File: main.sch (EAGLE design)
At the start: 44 parts, among them IC1 MEGA16-A, IC2 MCP73831, IC3 7805DT, Q2 32768k

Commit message: Schematics
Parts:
- added R22: 10k, rcl:R-EU_R1206
- added S1: MODE, switch-omron:10-XX
- JP1: value (none) -> 12V
- JP2: value (none) -> BAT 3.7V
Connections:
- new net N$38: IC1.(T0/XCK)PB0, R22.1, S1.S
- net +5V: now also R22.2
- net GND: now also S1.P
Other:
- moved on the sheet: D2, R20, R21
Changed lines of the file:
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@@
 <part name="T5" library="transistor" deviceset="*-PNP-" device="SOT23-BEC" technology="BC807-25"/>
 <part name="U$1" library="dallas-1" deviceset="DS1629" device=""/>
-<part name="JP1" library="pinhead" deviceset="PINHD-1X2" device=""/>
-<part name="JP2" library="pinhead" deviceset="PINHD-1X2" device=""/>
+<part name="JP1" library="pinhead" deviceset="PINHD-1X2" device="" value="12V"/>
+<part name="JP2" library="pinhead" deviceset="PINHD-1X2" device="" value="BAT 3.7V"/>
 <part name="IC2" library="microchip-update-2" deviceset="MCP73831" device=""/>
 <part name="IC3" library="linear" deviceset="78*" device="DT" technology="05"/>
@@
 <part name="T6" library="transistor" deviceset="*-NPN-" device="SOT23-EBC"/>
 <part name="D2" library="diode" deviceset="BZX84CSMD" device=""/>
+<part name="R22" library="rcl" deviceset="R-EU_" device="R1206" value="10k"/>
+<part name="GND9" library="supply1" deviceset="GND" device=""/>
+<part name="P+7" library="supply1" deviceset="+5V" device=""/>
+<part name="S1" library="switch-omron" deviceset="10-XX" device="" value="MODE"/>
 </parts>
 <sheets>
@@
 <instance part="R19" gate="G$1" x="246.38" y="33.02"/>
 <instance part="+3V2" gate="G$1" x="213.36" y="233.68"/>
-<instance part="R20" gate="G$1" x="213.36" y="154.94" rot="R90"/>
-<instance part="R21" gate="G$1" x="213.36" y="139.7" rot="R90"/>
+<instance part="R20" gate="G$1" x="218.44" y="195.58" rot="R90"/>
+<instance part="R21" gate="G$1" x="218.44" y="180.34" rot="R90"/>
 <instance part="P+4" gate="1" x="38.1" y="195.58"/>
-<instance part="P+5" gate="1" x="213.36" y="177.8"/>
-<instance part="GND8" gate="1" x="213.36" y="124.46"/>
+<instance part="P+5" gate="1" x="218.44" y="208.28"/>
+<instance part="GND8" gate="1" x="218.44" y="165.1"/>
 <instance part="P+6" gate="1" x="134.62" y="157.48"/>
 <instance part="D3" gate="G$1" x="33.02" y="180.34"/>
@@
 <instance part="D1" gate="G$1" x="45.72" y="160.02" rot="R90"/>
 <instance part="T6" gate="G$1" x="45.72" y="177.8" rot="R90"/>
-<instance part="D2" gate="G$1" x="220.98" y="139.7" rot="R90"/>
+<instance part="D2" gate="G$1" x="226.06" y="180.34" rot="R90"/>
+<instance part="R22" gate="G$1" x="213.36" y="142.24" rot="R90"/>
+<instance part="GND9" gate="1" x="213.36" y="111.76"/>
+<instance part="P+7" gate="1" x="213.36" y="154.94"/>
+<instance part="S1" gate="1" x="213.36" y="121.92"/>
 </instances>
 <busses>
@@
 <pinref part="GND8" gate="1" pin="GND"/>
 <pinref part="R21" gate="G$1" pin="1"/>
-<wire x1="213.36" y1="127" x2="213.36" y2="132.08" width="0.1524" layer="91"/>
-<wire x1="213.36" y1="132.08" x2="213.36" y2="134.62" width="0.1524" layer="91"/>
-<wire x1="220.98" y1="137.16" x2="220.98" y2="132.08" width="0.1524" layer="91"/>
-<wire x1="220.98" y1="132.08" x2="213.36" y2="132.08" width="0.1524" layer="91"/>
-<junction x="213.36" y="132.08"/>
+<wire x1="218.44" y1="167.64" x2="218.44" y2="172.72" width="0.1524" layer="91"/>
+<wire x1="218.44" y1="172.72" x2="218.44" y2="175.26" width="0.1524" layer="91"/>
+<wire x1="226.06" y1="177.8" x2="226.06" y2="172.72" width="0.1524" layer="91"/>
+<wire x1="226.06" y1="172.72" x2="218.44" y2="172.72" width="0.1524" layer="91"/>
+<junction x="218.44" y="172.72"/>
 <pinref part="D2" gate="G$1" pin="A"/>
+</segment>
+<segment>
+<pinref part="GND9" gate="1" pin="GND"/>
+<wire x1="213.36" y1="116.84" x2="213.36" y2="114.3" width="0.1524" layer="91"/>
+<pinref part="S1" gate="1" pin="P"/>
 </segment>
 </net>
@@
 <junction x="134.62" y="132.08"/>
 </segment>
+<segment>
+<pinref part="P+7" gate="1" pin="+5V"/>
+<pinref part="R22" gate="G$1" pin="2"/>
+<wire x1="213.36" y1="152.4" x2="213.36" y2="147.32" width="0.1524" layer="91"/>
+</segment>
 </net>
 <net name="N$8" class="0">
@@
 <pinref part="P+5" gate="1" pin="+12V"/>
 <pinref part="R20" gate="G$1" pin="2"/>
-<wire x1="213.36" y1="175.26" x2="213.36" y2="160.02" width="0.1524" layer="91"/>
+<wire x1="218.44" y1="205.74" x2="218.44" y2="200.66" width="0.1524" layer="91"/>
 </segment>
 <segment>
@@
 <pinref part="R21" gate="G$1" pin="2"/>
 <pinref part="R20" gate="G$1" pin="1"/>
-<wire x1="213.36" y1="144.78" x2="213.36" y2="147.32" width="0.1524" layer="91"/>
+<wire x1="218.44" y1="185.42" x2="218.44" y2="187.96" width="0.1524" layer="91"/>
 <pinref part="IC1" gate="G$1" pin="(ADC0)PA0"/>
-<wire x1="213.36" y1="147.32" x2="213.36" y2="149.86" width="0.1524" layer="91"/>
-<wire x1="193.04" y1="134.62" x2="203.2" y2="134.62" width="0.1524" layer="91"/>
-<wire x1="203.2" y1="134.62" x2="203.2" y2="147.32" width="0.1524" layer="91"/>
-<wire x1="203.2" y1="147.32" x2="213.36" y2="147.32" width="0.1524" layer="91"/>
-<junction x="213.36" y="147.32"/>
-<wire x1="213.36" y1="147.32" x2="220.98" y2="147.32" width="0.1524" layer="91"/>
-<wire x1="220.98" y1="147.32" x2="220.98" y2="142.24" width="0.1524" layer="91"/>
+<wire x1="218.44" y1="187.96" x2="218.44" y2="190.5" width="0.1524" layer="91"/>
+<wire x1="193.04" y1="134.62" x2="198.12" y2="134.62" width="0.1524" layer="91"/>
+<wire x1="198.12" y1="134.62" x2="198.12" y2="187.96" width="0.1524" layer="91"/>
+<wire x1="198.12" y1="187.96" x2="218.44" y2="187.96" width="0.1524" layer="91"/>
+<junction x="218.44" y="187.96"/>
+<wire x1="218.44" y1="187.96" x2="226.06" y2="187.96" width="0.1524" layer="91"/>
+<wire x1="226.06" y1="187.96" x2="226.06" y2="182.88" width="0.1524" layer="91"/>
 <pinref part="D2" gate="G$1" pin="C"/>
 </segment>
@@
 <wire x1="124.46" y1="218.44" x2="129.54" y2="218.44" width="0.1524" layer="91"/>
 <wire x1="124.46" y1="218.44" x2="124.46" y2="170.18" width="0.1524" layer="91"/>
-<wire x1="124.46" y1="170.18" x2="198.12" y2="170.18" width="0.1524" layer="91"/>
+<wire x1="124.46" y1="170.18" x2="195.58" y2="170.18" width="0.1524" layer="91"/>
 <pinref part="IC1" gate="G$1" pin="(ADC7)PA7"/>
-<wire x1="198.12" y1="170.18" x2="198.12" y2="152.4" width="0.1524" layer="91"/>
-<wire x1="198.12" y1="152.4" x2="193.04" y2="152.4" width="0.1524" layer="91"/>
+<wire x1="195.58" y1="170.18" x2="195.58" y2="152.4" width="0.1524" layer="91"/>
+<wire x1="195.58" y1="152.4" x2="193.04" y2="152.4" width="0.1524" layer="91"/>
 </segment>
 </net>
@@
 </segment>
 </net>
+<net name="N$38" class="0">
+<segment>
+<pinref part="R22" gate="G$1" pin="1"/>
+<wire x1="213.36" y1="137.16" x2="213.36" y2="132.08" width="0.1524" layer="91"/>
+<pinref part="IC1" gate="G$1" pin="(T0/XCK)PB0"/>
+<wire x1="213.36" y1="132.08" x2="213.36" y2="127" width="0.1524" layer="91"/>
+<wire x1="193.04" y1="111.76" x2="203.2" y2="111.76" width="0.1524" layer="91"/>
+<wire x1="203.2" y1="111.76" x2="203.2" y2="132.08" width="0.1524" layer="91"/>
+<wire x1="203.2" y1="132.08" x2="213.36" y2="132.08" width="0.1524" layer="91"/>
+<junction x="213.36" y="132.08"/>
+<pinref part="S1" gate="1" pin="S"/>
+</segment>
+</net>

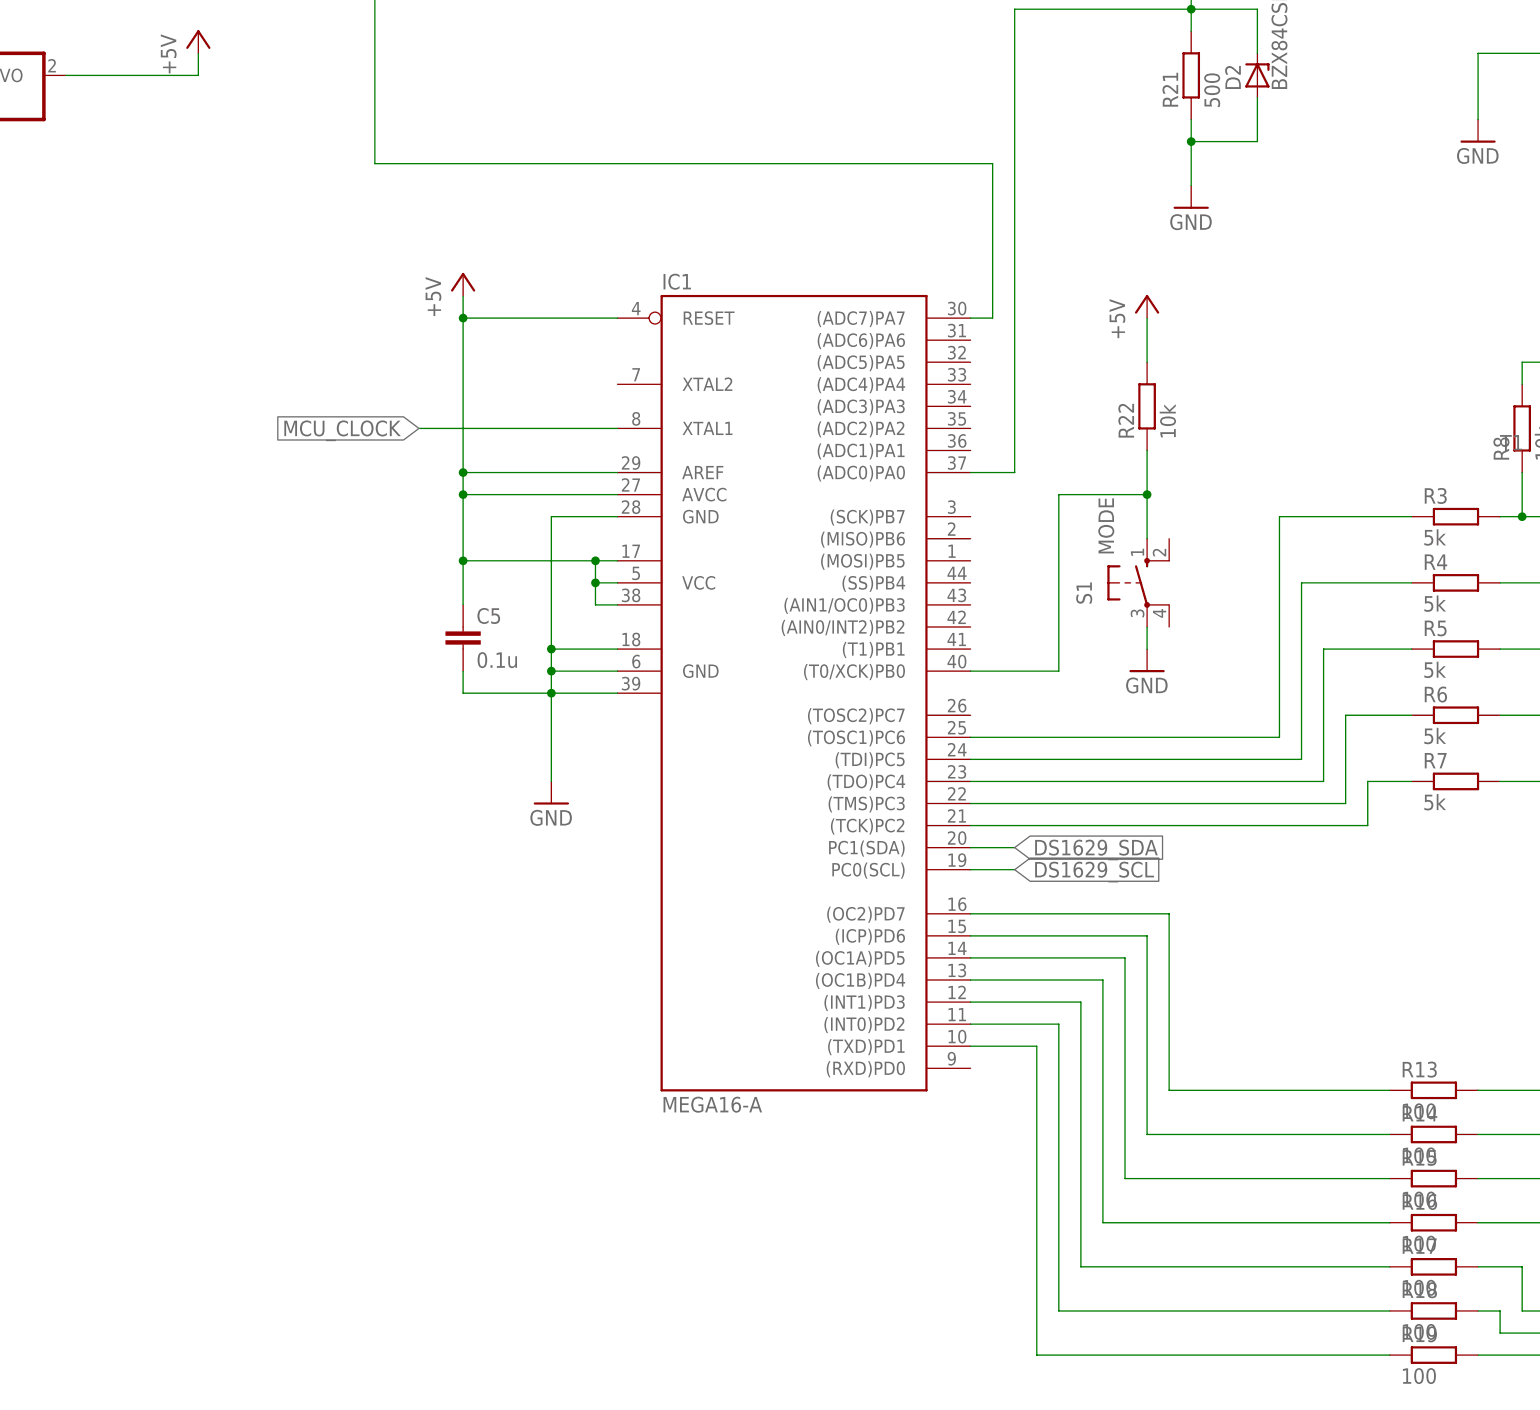
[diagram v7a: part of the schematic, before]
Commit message: Atmega8 instead of Atmega16
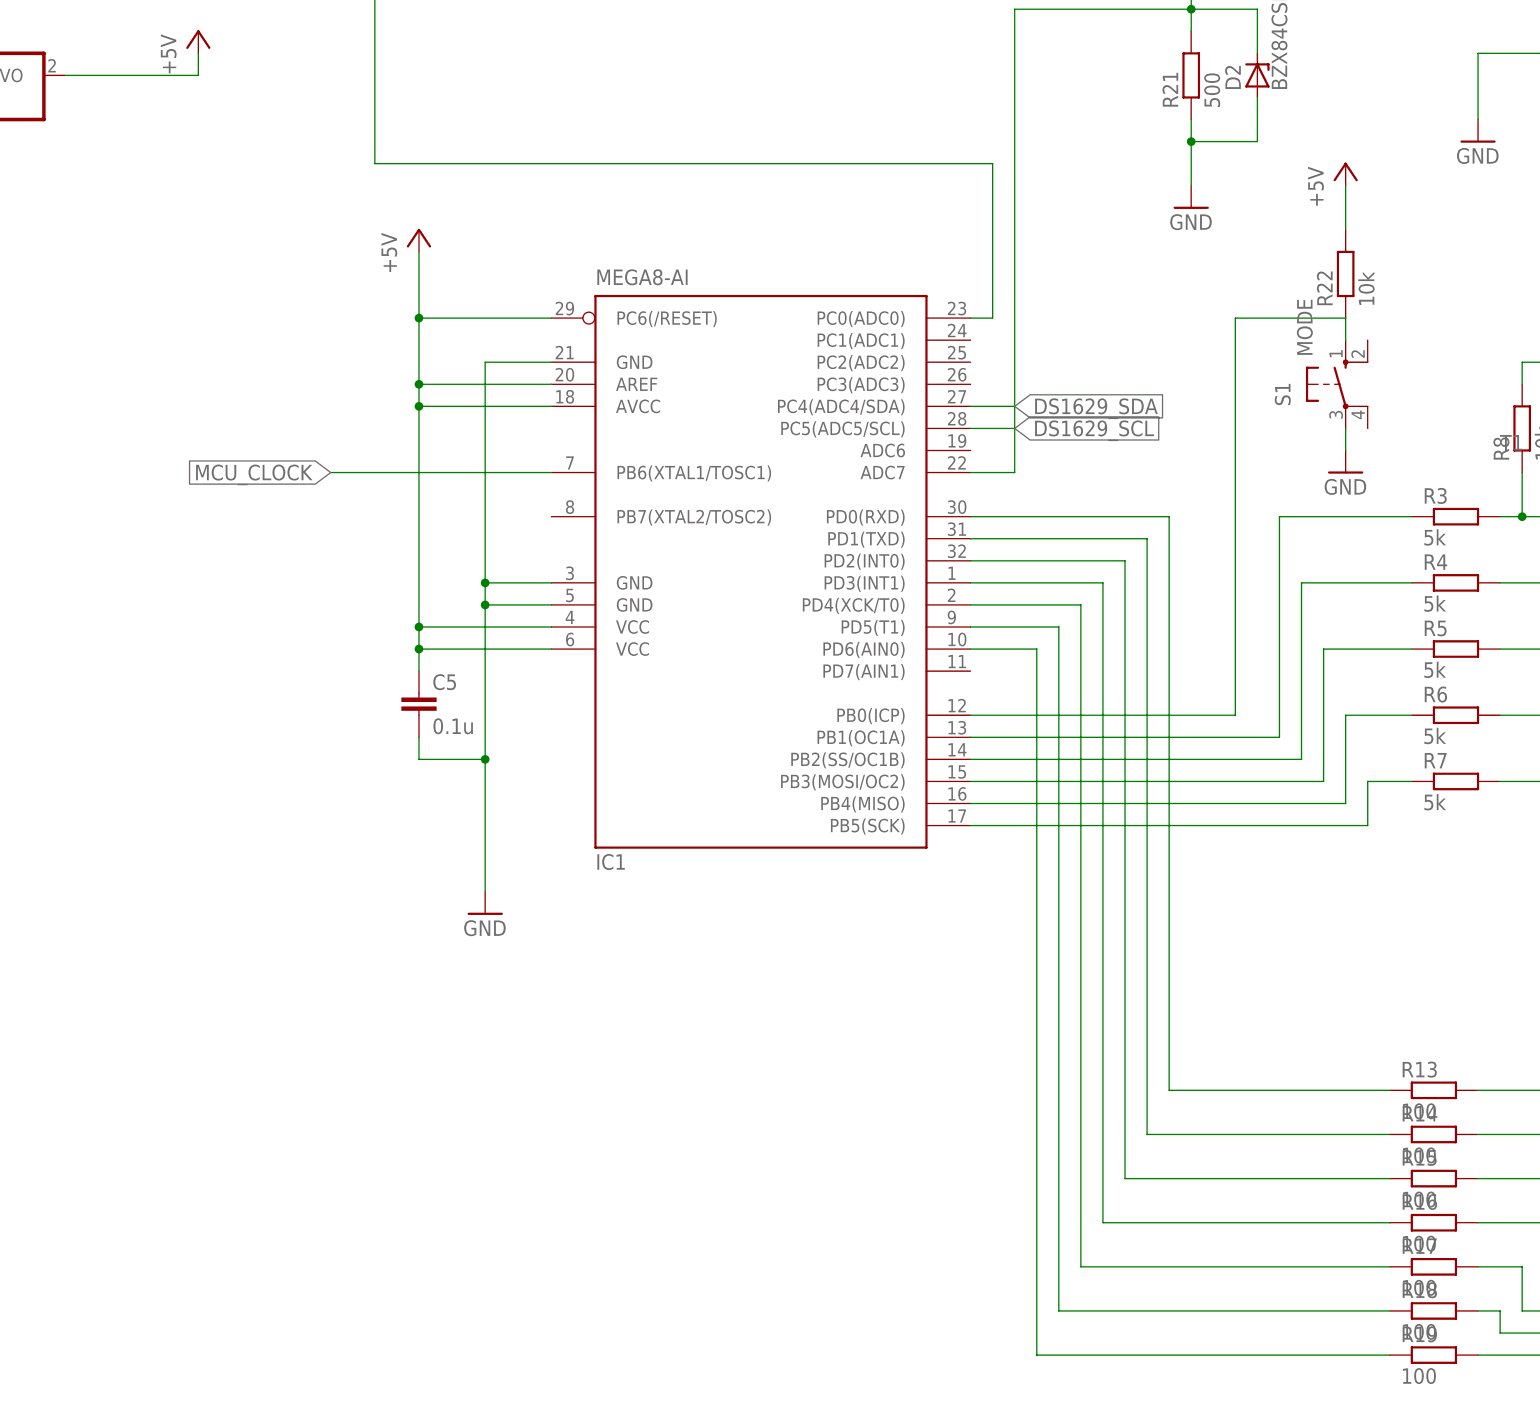
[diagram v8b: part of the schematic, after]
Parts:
- IC1: value MEGA16-A -> MEGA8-AI; device atmel:MEGA16-A -> atmel:MEGA8-AI
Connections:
- net +5V: now also IC1.PC6(/RESET), IC1.VCC@1, IC1.VCC@2; no longer IC1.RESET, IC1.VCC, IC1.VCC1, IC1.VCC2
- net DS1629_SCL: no longer IC1.PC0(SCL)
- net DS1629_SDA: no longer IC1.PC1(SDA)
- net GND: now also IC1.GND@2; no longer IC1.GND1, IC1.GND2
- net MCU_CLOCK: now also IC1.PB6(XTAL1/TOSC1); no longer IC1.XTAL1
- net N$19: no longer IC1.(INT1)PD3
- net N$20: no longer IC1.(OC2)PD7
- net N$21: no longer IC1.(ICP)PD6
- net N$22: no longer IC1.(OC1A)PD5
- net N$23: now also IC1.PB1(OC1A); no longer IC1.(TOSC1)PC6
- net N$24: now also IC1.PB2(SS/OC1B); no longer IC1.(TDI)PC5
- net N$25: now also IC1.PB3(MOSI/OC2); no longer IC1.(TDO)PC4
- net N$26: now also IC1.PB4(MISO); no longer IC1.(TMS)PC3
- net N$27: now also IC1.PB5(SCK); no longer IC1.(TCK)PC2
- net N$3: now also IC1.ADC7; no longer IC1.(ADC0)PA0
- net N$30: no longer IC1.(OC1B)PD4
- net N$35: no longer IC1.(INT0)PD2
- net N$36: no longer IC1.(TXD)PD1
- net N$38: now also IC1.PB0(ICP); no longer IC1.(T0/XCK)PB0
- net N$4: now also IC1.PC0(ADC0); no longer IC1.(ADC7)PA7
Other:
- moved on the sheet: C5, R22, S1
